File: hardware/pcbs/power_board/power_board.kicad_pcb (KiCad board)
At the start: 2 copper layers, 90 x 90 mm, 144 parts, among them J1 Header_01x04, J10 Molex 254 47053, J11 Molex 254 47053, J12 Molex 254 47053, J13 Molex 254 47053, J14 Header_02x03, J15 PJ-102AH, J16 ScrewTerminal_02, J17 ScrewTerminal_02, J18 ScrewTerminal_02, J19 ScrewTerminal_02, J2 Header_01x04, J20 ScrewTerminal_02, J21 Header_02x04, J22 ScrewTerminal_02, J3 USB3_B_Micro, J4 USB3_A, J5 USB_A, J6 USB_A, J7 USB_A, J8 USB_A, J9 Molex 254 47053, Q1 BSS138, Q2 BSS138, Q3 BSS138, Q4 BSS138, Q5 IRFR5305, U1 VRB1205S-6WR3, U10 EMC2305, U11 TCA9534, U12 LMR38020, U13 LMR38020, U14 TMP1075D, U2 LTV-247, U3 NCP380, U4 VRB1205S-6WR3, U5 NCP380, U6 VRB1205S-6WR3, U7 NCP380, U8 VRB1205S-6WR3, U9 NCP380

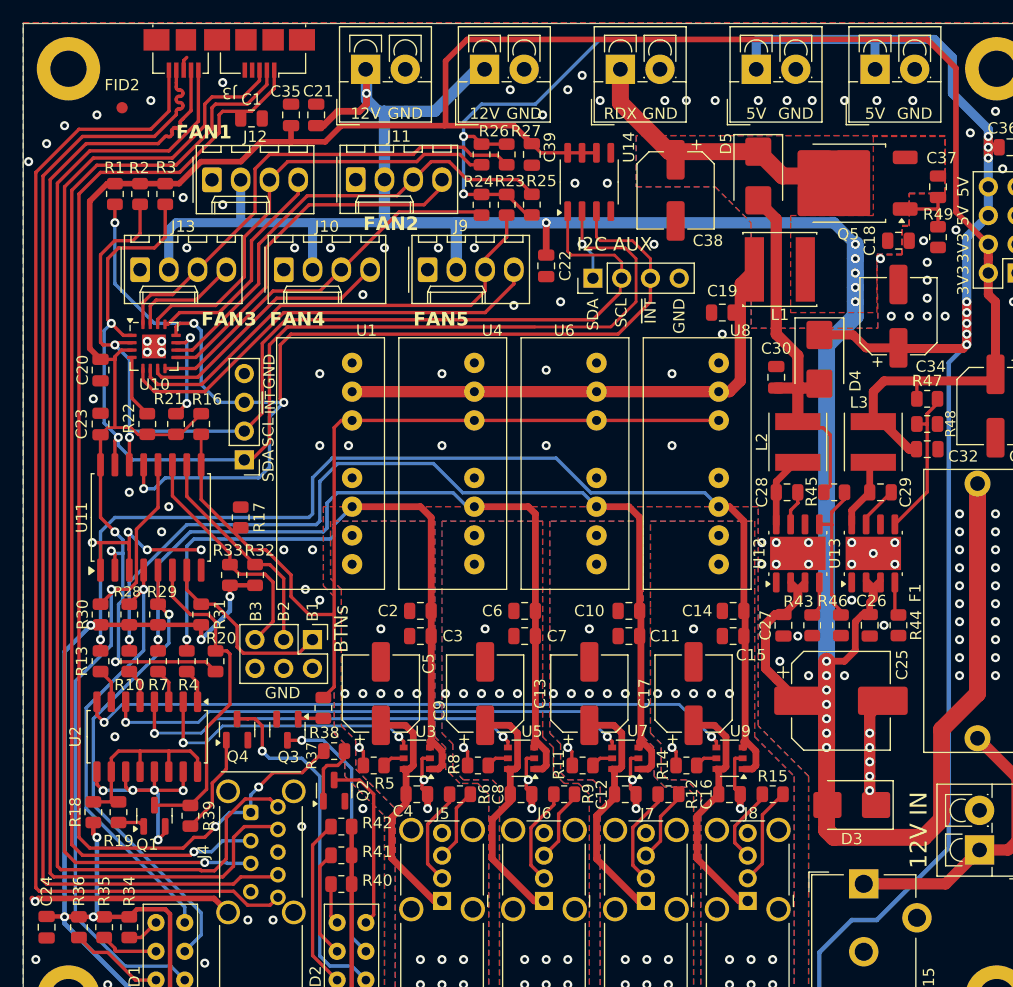
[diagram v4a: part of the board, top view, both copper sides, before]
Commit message: Re-route the usb3 differential pairs
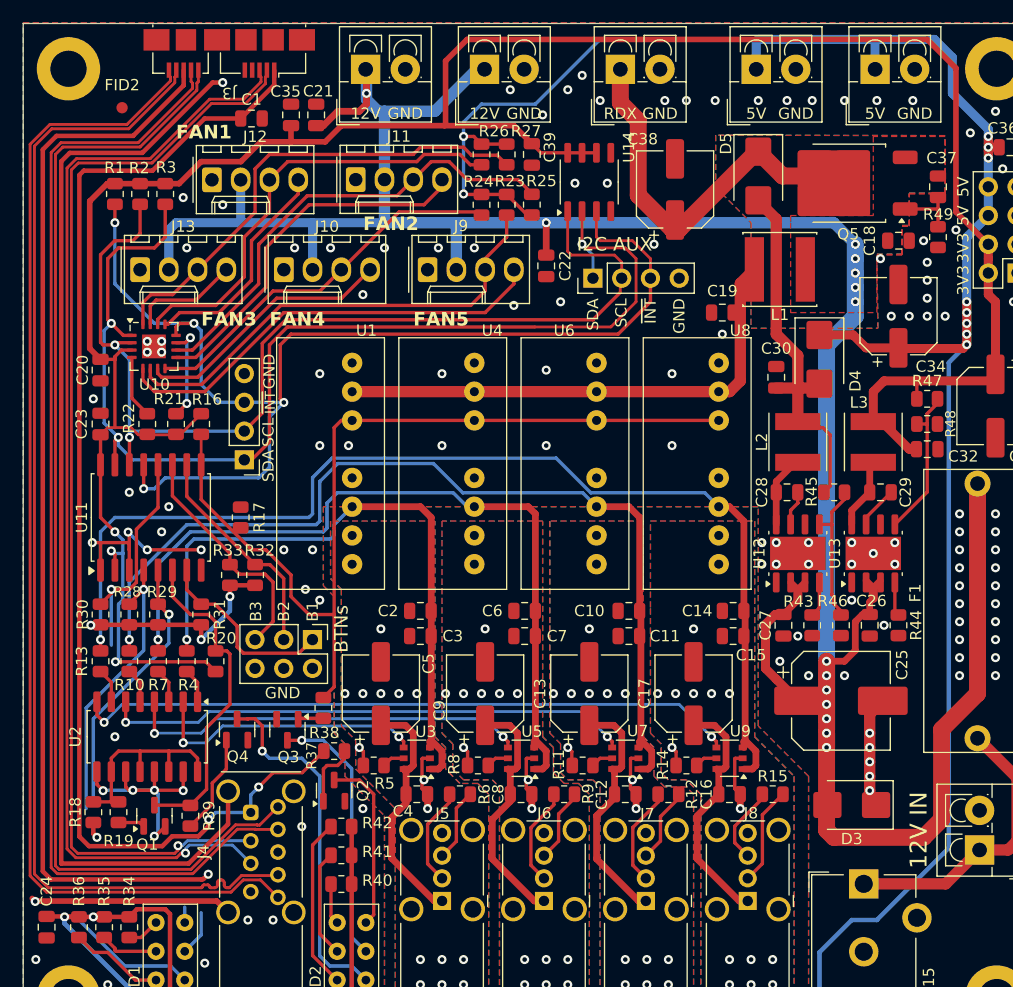
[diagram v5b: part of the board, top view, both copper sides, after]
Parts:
- moved C38 0.10 mm to (87.6, 98.7), turned to 90 degrees
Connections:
- net Net-(J3-D+) renamed /USB Passthrough/D+
- net Net-(J3-D-) renamed /USB Passthrough/D-
- net Net-(J3-SSRX+) renamed /USB Passthrough/SSRX+
- net Net-(J3-SSRX-) renamed /USB Passthrough/SSRX-
- net Net-(J3-SSTX+) renamed /USB Passthrough/SSTX+
- net Net-(J3-SSTX-) renamed /USB Passthrough/SSTX-
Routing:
- net GND: track 69.0 -> 260.5 mm, vias 138 -> 134
- net +5V: track 362.5 -> 328.7 mm
- net /GPIOs/LED3: track 57.5 -> 32.3 mm
- net /GPIOs/LED2: track 41.4 -> 28.0 mm
- net /GPIOs/LED1: track 38.7 -> 26.4 mm
- net Net-(D5-K): track 22.6 -> 32.1 mm
- net /USB Passthrough/SSTX-: track 104.2 -> 101.6 mm
- net /USB Passthrough/SSTX+: track 104.2 -> 101.6 mm
- net /USB Passthrough/SSRX-: track 102.9 -> 103.9 mm
- net /USB Passthrough/SSRX+: track 103.1 -> 103.9 mm
- net /USB Passthrough/D+: track 98.8 -> 99.4 mm

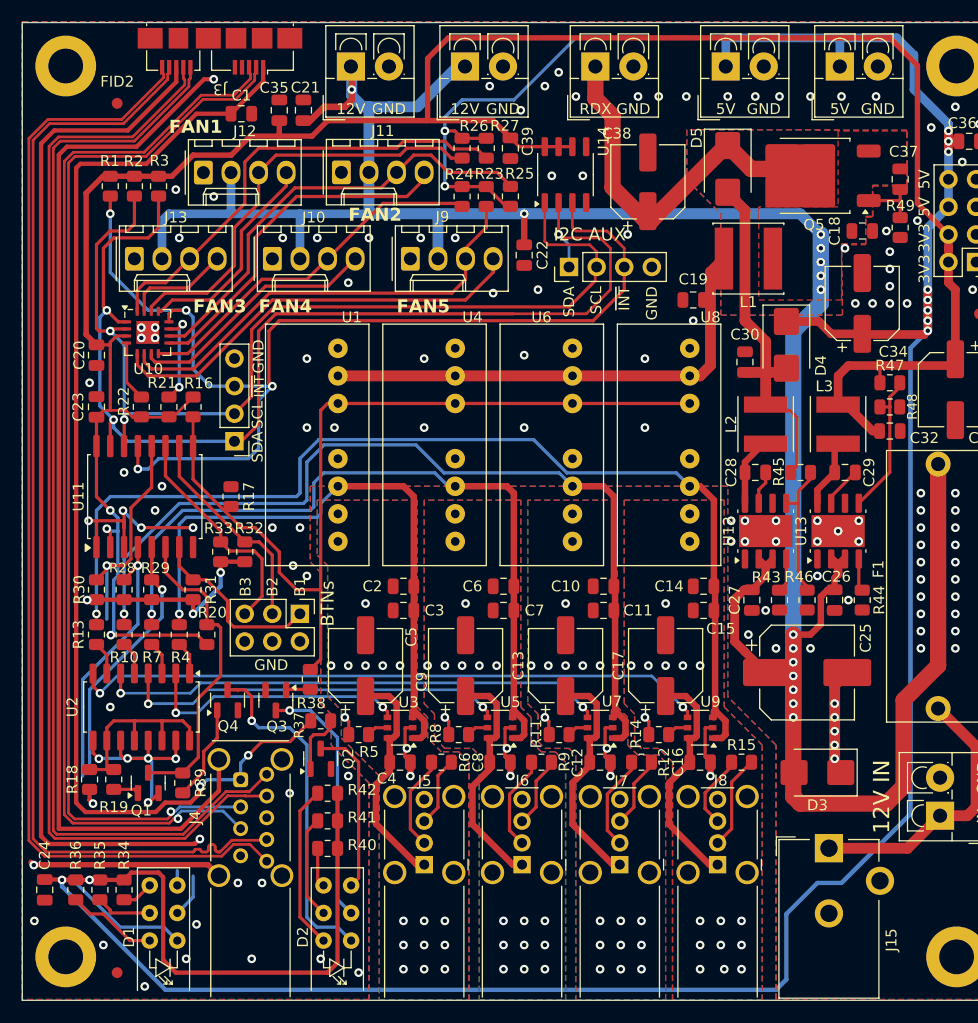
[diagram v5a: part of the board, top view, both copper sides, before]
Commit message: power_board: fix some inconsistencies
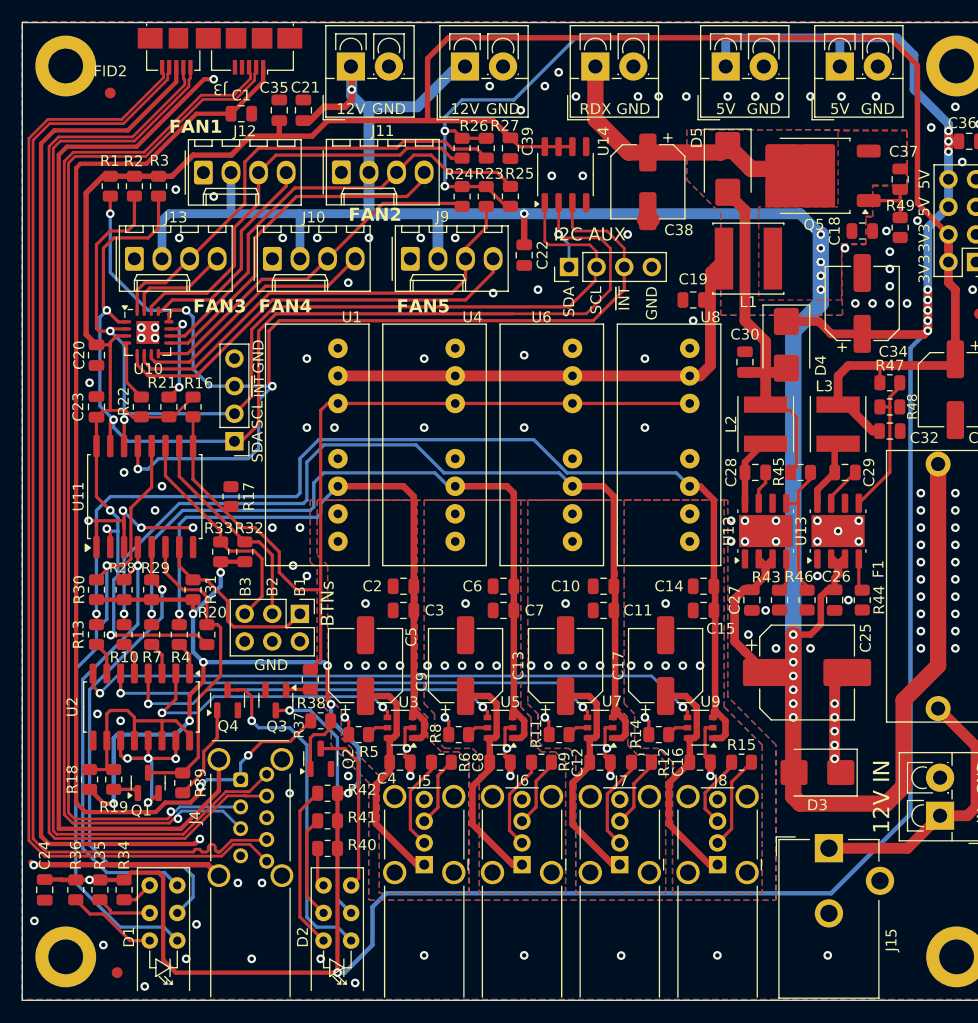
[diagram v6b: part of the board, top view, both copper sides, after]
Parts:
- moved FID2 1.14 mm to (38.1, 90.5)
- turned C38 to -90 degrees
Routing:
- net /GPIOs/LED3: track 32.3 -> 57.3 mm
- net +5V: track 328.7 -> 347.9 mm, vias 16 -> 20
- net /GPIOs/LED2: track 28.0 -> 45.3 mm
- net /GPIOs/LED1: track 26.4 -> 41.8 mm
- net Net-(D5-K): track 32.1 -> 24.4 mm
- net GND: track 260.5 -> 256.6 mm, vias 134 -> 139
- net Net-(U3-~{FLAG}): track 24.8 -> 26.6 mm
- net /Isolated chargers/Isolated charger 1/~{OVERCURRENT}: track 19.0 -> 20.4 mm
- net /Isolated chargers/Isolated charger 4/GND-CHG: vias 18 -> 9
- net /Isolated chargers/Isolated charger 3/GND-CHG: vias 17 -> 8
- net /Isolated chargers/Isolated charger 2/GND-CHG: vias 18 -> 9
- net /Isolated chargers/Isolated charger 1/GND-CHG: vias 18 -> 8

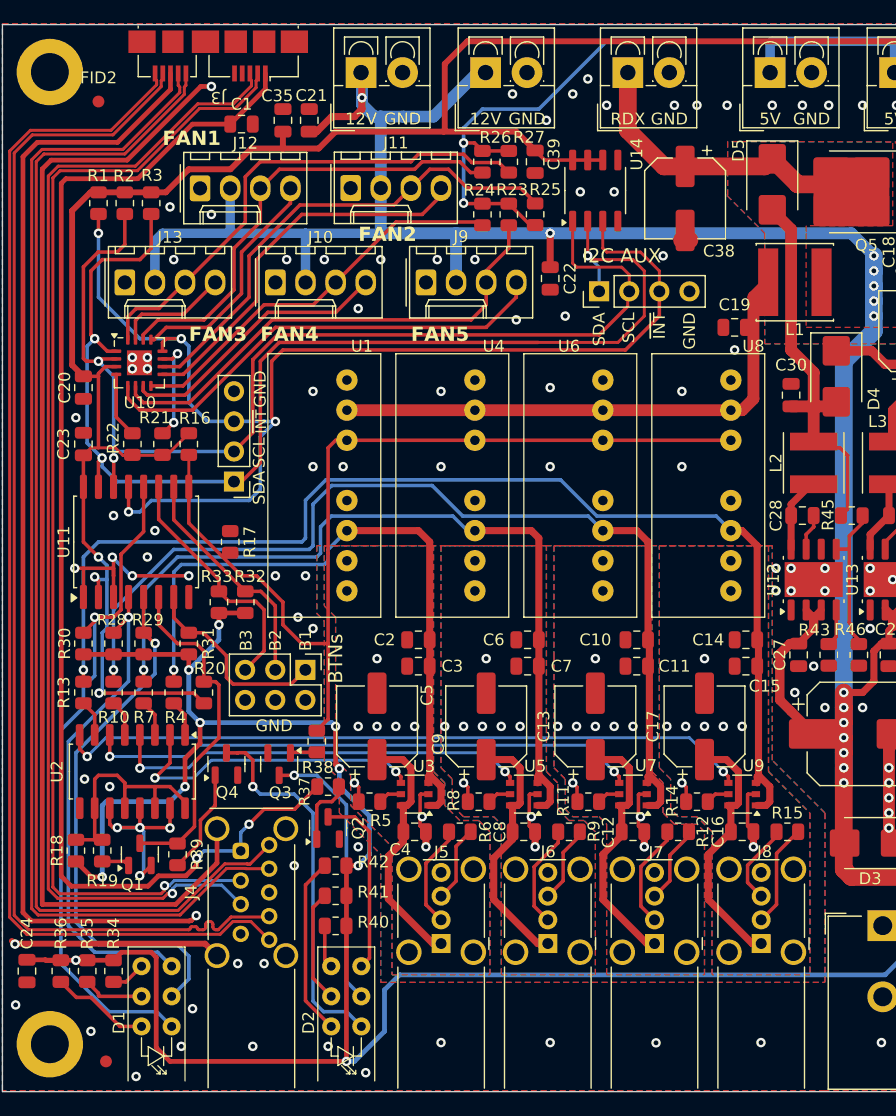
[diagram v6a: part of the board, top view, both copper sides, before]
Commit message: power_board: fix DRC issues
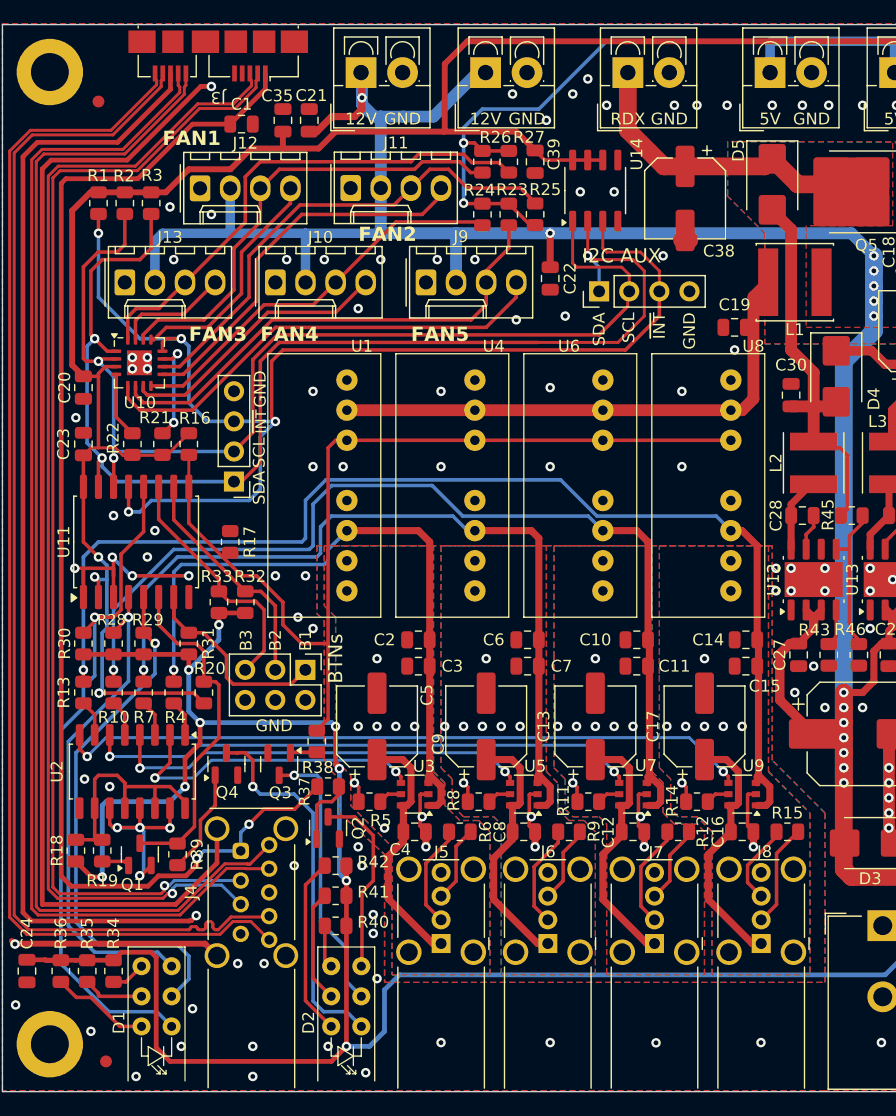
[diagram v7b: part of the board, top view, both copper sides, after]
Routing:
- net +5V: track 347.9 -> 347.0 mm, vias 20 -> 19
- net GND: vias 139 -> 144
- net /Isolated chargers/Isolated charger 1/GND-CHG: vias 8 -> 9

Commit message: power_board: final version
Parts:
- D5: value a nice diode -> S2A
- moved FID1 14.6 mm to (104.1, 114.9)
- moved FID2 0.32 mm to (38.1, 90.2)
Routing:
- net /GPIOs/LED1: track 41.8 -> 42.9 mm
- net /GPIOs/LED2: track 45.3 -> 46.3 mm
